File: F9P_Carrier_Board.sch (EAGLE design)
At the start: 82 parts, among them J4 U.FL, J5 QWIIC_RIGHT_ANGLE, J6 MICROMOD-2222-C, J8 JTAG, U1 U-BLOX_ZED-F9P, U5 AP7361C-33

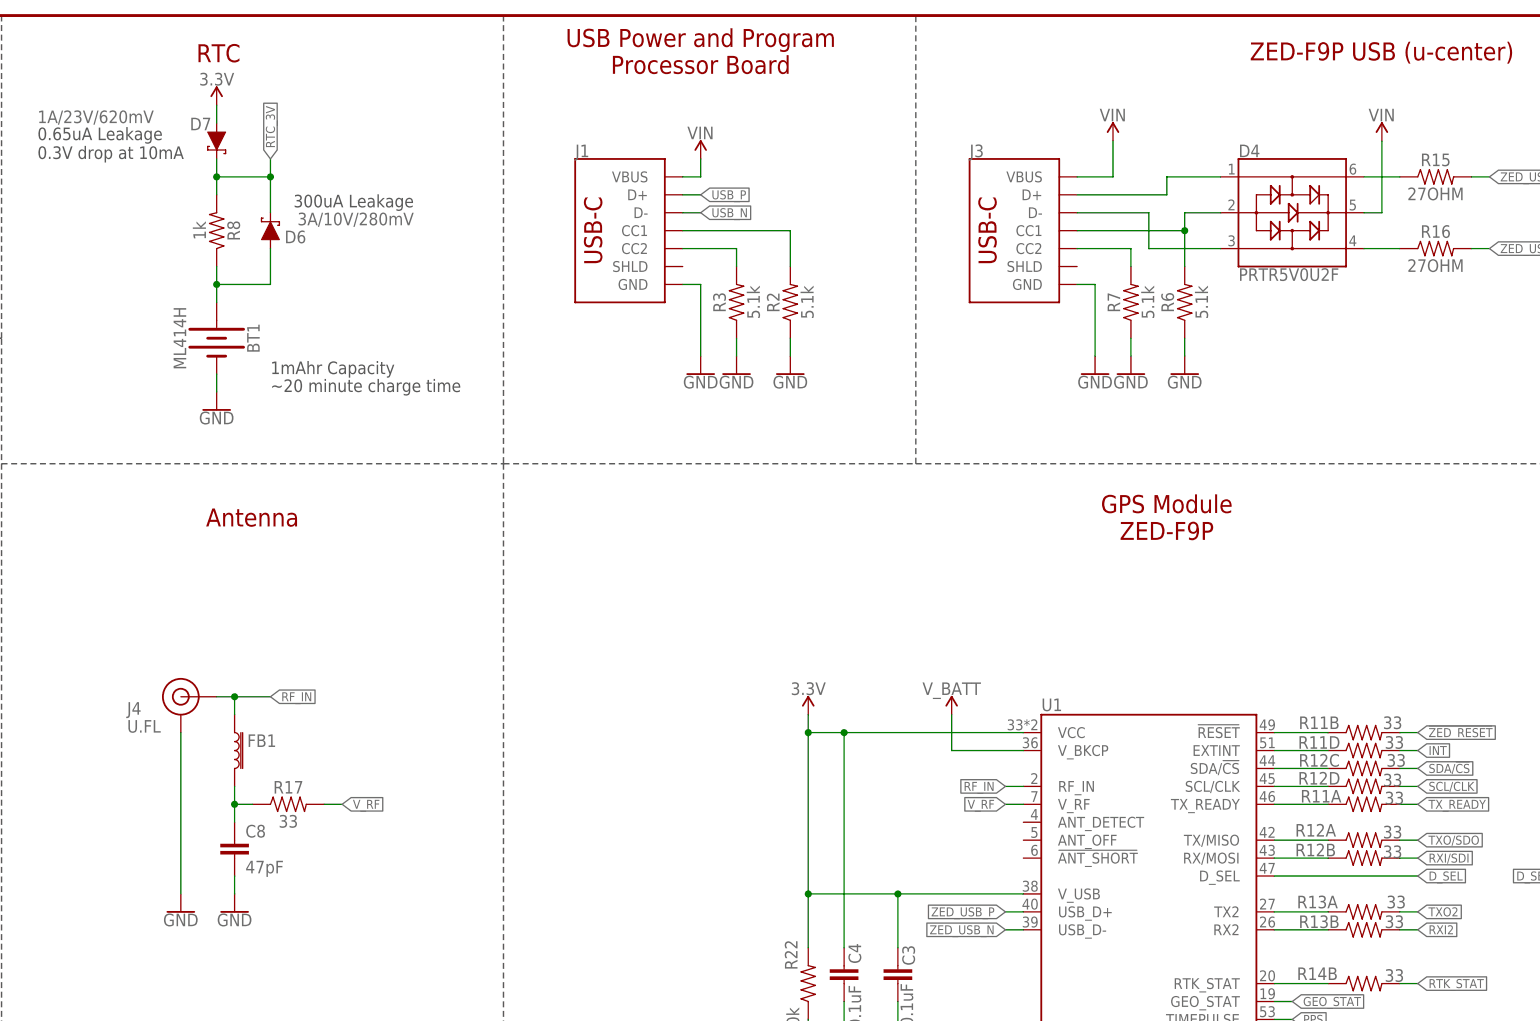
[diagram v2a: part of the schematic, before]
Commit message: Puts parts generally where they will be routed
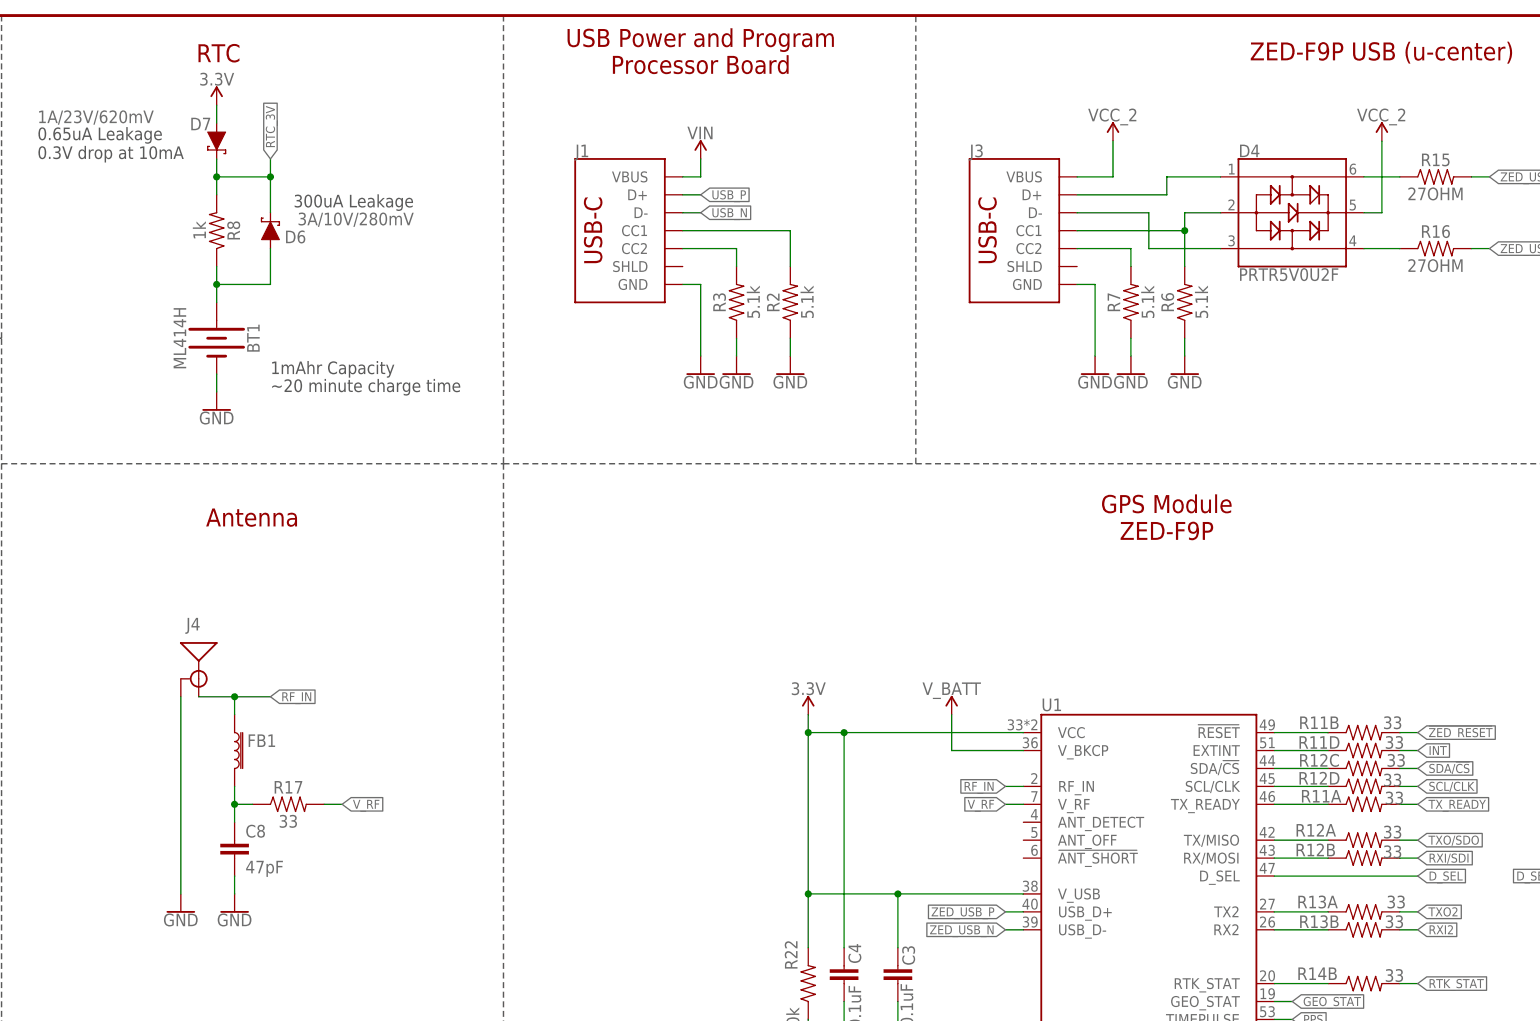
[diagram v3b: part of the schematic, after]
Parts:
- J4: device SparkFun-Connectors:U.FL2PIN -> SparkFun-RF:ANTENNA-GROUNDEDEDGE_SMA_SMD
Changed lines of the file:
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@@
 <part name="R14" library="SparkFun-Resistors" deviceset="33OHM_RA" device="-1206-1/16W-5%" value="33"/>
 <part name="SUPPLY2" library="SparkFun-PowerSymbols" deviceset="VIN" device=""/>
-<part name="SUPPLY3" library="SparkFun-PowerSymbols" deviceset="VIN" device=""/>
+<part name="SUPPLY3" library="SparkFun-PowerSymbols" deviceset="VCC_2" device=""/>
 <part name="R15" library="SparkFun-Resistors" deviceset="27OHM" device=""/>
 <part name="R16" library="SparkFun-Resistors" deviceset="27OHM" device=""/>
 <part name="D4" library="SparkFun-IC-Power" deviceset="PRTR5V0U2" device="F"/>
-<part name="SUPPLY5" library="SparkFun-PowerSymbols" deviceset="VIN" device=""/>
-<part name="J4" library="SparkFun-Connectors" deviceset="U.FL2PIN" device="" value="U.FL"/>
+<part name="SUPPLY5" library="SparkFun-PowerSymbols" deviceset="VCC_2" device=""/>
+<part name="J4" library="SparkFun-RF" deviceset="ANTENNA-GROUNDED" device="EDGE_SMA_SMD" value="U.FL"/>
 <part name="GND14" library="SparkFun-PowerSymbols" deviceset="GND" device=""/>
 <part name="GND17" library="SparkFun-PowerSymbols" deviceset="GND" device=""/>
@@
 <attribute name="VALUE" x="363.22" y="264.414" size="1.778" layer="96" align="bottom-center"/>
 </instance>
-<instance part="J4" gate="G$1" x="193.04" y="182.88" smashed="yes">
-<attribute name="NAME" x="185.42" y="180.34" size="1.778" layer="95"/>
-<attribute name="VALUE" x="185.42" y="177.8" size="1.778" layer="96"/>
+<instance part="J4" gate="G$1" x="195.58" y="185.42" smashed="yes" rot="MR0">
+<attribute name="NAME" x="195.834" y="192.278" size="1.778" layer="95" rot="MR0"/>
 </instance>
 <instance part="GND14" gate="1" x="193.04" y="152.4" smashed="yes">
@@
 <pinref part="J4" gate="G$1" pin="GND"/>
 <pinref part="GND14" gate="1" pin="GND"/>
-<wire x1="193.04" y1="177.8" x2="193.04" y2="154.94" width="0.1524" layer="91"/>
+<wire x1="193.04" y1="182.88" x2="193.04" y2="154.94" width="0.1524" layer="91"/>
 </segment>
 <segment>
@@
 <wire x1="320.04" y1="256.54" x2="325.12" y2="256.54" width="0.1524" layer="91"/>
 <wire x1="325.12" y1="256.54" x2="325.12" y2="261.62" width="0.1524" layer="91"/>
-<pinref part="SUPPLY3" gate="G$1" pin="VIN"/>
+<pinref part="SUPPLY3" gate="G$1" pin="VCC_2"/>
 </segment>
 <segment>
@@
 <wire x1="360.68" y1="251.46" x2="363.22" y2="251.46" width="0.1524" layer="91"/>
 <wire x1="363.22" y1="251.46" x2="363.22" y2="261.62" width="0.1524" layer="91"/>
-<pinref part="SUPPLY5" gate="G$1" pin="VIN"/>
+<pinref part="SUPPLY5" gate="G$1" pin="VCC_2"/>
 </segment>
 <segment>
@@
 <wire x1="200.66" y1="180.34" x2="200.66" y2="182.88" width="0.1524" layer="91"/>
 <pinref part="J4" gate="G$1" pin="SIGNAL"/>
-<wire x1="200.66" y1="182.88" x2="198.12" y2="182.88" width="0.1524" layer="91"/>
+<wire x1="200.66" y1="182.88" x2="195.58" y2="182.88" width="0.1524" layer="91"/>
 <junction x="200.66" y="182.88"/>
 <pinref part="FB1" gate="G$1" pin="1"/>

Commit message: Still situating the parts within the  board
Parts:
- removed J7: (no value), SparkFun-Connectors:CONN_08NO_SILK_DNP
- removed R14: 33, SparkFun-Resistors:33OHM_RA-1206-1/16W-5%
- J10: device SparkFun-Connectors:CONN_09NO_SILK -> SparkFun-Connectors:CONN_121X12_NO_SILK_KIT
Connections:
- removed net N$30: R14B.1, U1.RTK_STAT
- net 3.3V: now also J10.9, J9.3; no longer J10.8, J7.3
- net GND: now also J10.10; no longer J10.9, J7.1, J7.8
- net N$15: now also R11A.1, U1.EXTINT; no longer R11B.1, U1.!RESET!
- net N$16: now also R11B.1, U1.!SAFEBOOT!; no longer R11D.1, U1.EXTINT
- net N$19: now also R11C.1, U1.!RESET!; no longer R11A.1, U1.TX_READY
- net N$20: now also R11D.1, U1.TX_READY; no longer R11C.1, U1.!SAFEBOOT!
- net N$21: now also R12A.1, U1.SCL/CLK; no longer R12C.1, U1.SDA/!CS!
- net N$22: now also R12B.1, U1.SDA/!CS!; no longer R12D.1, U1.SCL/CLK
- net N$23: now also R12C.1, U1.RX/MOSI; no longer R12A.1, U1.TX/MISO
- net N$24: now also R12D.1, U1.TX/MISO; no longer R12B.1, U1.RX/MOSI
- net RTK_STAT: now also U1.RTK_STAT; no longer R14B.2
- net RXI/SDI: now also J10.11; no longer J7.5
- net SCL/CLK: now also J10.7; no longer J10.6, J7.7
- net SDA/!CS!: now also J10.8; no longer J10.7, J7.4
- net TXO/SDO: now also J10.12; no longer J7.6
- net VIN: now also J10.6; no longer J7.2
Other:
- moved on the sheet: R11A, R11B, R11C, R11D, R12A, R12B, R12C, R12D

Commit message: Moves parts to their final resting places (mostly)
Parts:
- C3, C4: device SparkFun-Capacitors:0.1UF-0402T-6.3V-10%-X7R -> SparkFun-Capacitors:0.1UF-0603-25V-5%
- C8: device SparkFun-Capacitors:47PF-0402-25V-5%-X7R -> SparkFun-Capacitors:47PF-0603-50V-5%
- R19, R20, R21: value 1KOHM-0402-1/16W-1% -> 1k; device SparkFun-Resistors:1KOHM-0402-1/16W-1% -> SparkFun-Resistors:1KOHM-0603-1/10W-1%
- R22: device SparkFun-Resistors:100KOHM-0402T-1/16W-1% -> SparkFun-Resistors:100KOHM-0603-1/10W-1%
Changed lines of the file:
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@@
 <part name="GND14" library="SparkFun-PowerSymbols" deviceset="GND" device=""/>
 <part name="GND17" library="SparkFun-PowerSymbols" deviceset="GND" device=""/>
-<part name="C8" library="SparkFun-Capacitors" deviceset="47PF" device="-0402-25V-5%-X7R" value="47pF"/>
+<part name="C8" library="SparkFun-Capacitors" deviceset="47PF" device="-0603-50V-5%" value="47pF"/>
 <part name="R17" library="SparkFun-Resistors" deviceset="33OHM" device="-0603-1/10W-1%" value="33"/>
 <part name="FB1" library="SparkFun-Coils" deviceset="FERRITE_BEAD-120_OHM" device="-0402T" value="FERRITE_BEAD-120_OHM-0402T"/>
-<part name="R19" library="SparkFun-Resistors" deviceset="1KOHM" device="-0402-1/16W-1%"/>
-<part name="R20" library="SparkFun-Resistors" deviceset="1KOHM" device="-0402-1/16W-1%"/>
+<part name="R19" library="SparkFun-Resistors" deviceset="1KOHM" device="-0603-1/10W-1%" value="1k"/>
+<part name="R20" library="SparkFun-Resistors" deviceset="1KOHM" device="-0603-1/10W-1%" value="1k"/>
 <part name="RTK" library="SparkFun-Jumpers" deviceset="JUMPER-SMT_2_NC_TRACE" device="_SILK" package3d_urn="urn:adsk.eagle:package:39281/1" value="JUMPER-SMT_2_NC_TRACE_SILK"/>
 <part name="PPS" library="SparkFun-Jumpers" deviceset="JUMPER-SMT_2_NC_TRACE" device="_SILK" package3d_urn="urn:adsk.eagle:package:39281/1" value="JUMPER-SMT_2_NC_TRACE_SILK"/>
@@
 <part name="D8" library="SparkFun-LED" deviceset="LED-BLUE" device="0603" value="BLUE"/>
 <part name="D9" library="SparkFun-LED" deviceset="LED-BLUE" device="0603" value="BLUE"/>
-<part name="R21" library="SparkFun-Resistors" deviceset="1KOHM" device="-0402-1/16W-1%"/>
+<part name="R21" library="SparkFun-Resistors" deviceset="1KOHM" device="-0603-1/10W-1%" value="1k"/>
 <part name="GEOF" library="SparkFun-Jumpers" deviceset="JUMPER-SMT_2_NC_TRACE" device="_SILK" package3d_urn="urn:adsk.eagle:package:39281/1" value="JUMPER-SMT_2_NC_TRACE_SILK"/>
 <part name="D10" library="SparkFun-LED" deviceset="LED-BLUE" device="0603" value="BLUE"/>
@@
 <part name="SUPPLY21" library="SparkFun-PowerSymbols" deviceset="3.3V" device=""/>
 <part name="BT2" library="SparkFun-Batteries" deviceset="ML414H_IV01E_BATTERY" device=""/>
-<part name="R22" library="SparkFun-Resistors" deviceset="100KOHM" device="-0402T-1/16W-1%" value="100k"/>
+<part name="R22" library="SparkFun-Resistors" deviceset="100KOHM" device="-0603-1/10W-1%" value="100k"/>
 <part name="GND29" library="SparkFun-PowerSymbols" deviceset="GND" device=""/>
 <part name="SUPPLY13" library="SparkFun-PowerSymbols" deviceset="3.3V" device=""/>
 <part name="SUPPLY22" library="SparkFun-PowerSymbols" deviceset="V_BATT" device=""/>
-<part name="C3" library="SparkFun-Capacitors" deviceset="0.1UF" device="-0402T-6.3V-10%-X7R" value="0.1uF"/>
-<part name="C4" library="SparkFun-Capacitors" deviceset="0.1UF" device="-0402T-6.3V-10%-X7R" value="0.1uF"/>
+<part name="C3" library="SparkFun-Capacitors" deviceset="0.1UF" device="-0603-25V-5%" value="0.1uF"/>
+<part name="C4" library="SparkFun-Capacitors" deviceset="0.1UF" device="-0603-25V-5%" value="0.1uF"/>
 <part name="LOGO1" library="SparkFun-Aesthetics" deviceset="SFE_LOGO_NAME" device=".1_INCH"/>
 <part name="FD2" library="SparkFun-Aesthetics" deviceset="FIDUCIAL" device="UFIDUCIAL"/>

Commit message: Routes more air wires - almost done
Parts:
- removed TP3: TEST-POINT3X5, SparkFun-Connectors:TEST-POINT3X5
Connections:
- removed net !SAFEBOOT: J10.3
- removed net GEOF_STAT: D10.A
- net !SAFEBOOT!: now also J10.3
- net GEO_STAT: now also D10.A
- net GND: now also D4.2
- net N$12: now also D4.3; no longer D4.1
- net N$13: now also D4.1; no longer D4.3
- net N$17: now also R15.1; no longer R16.1
- net N$6: no longer D4.2
- net N$9: now also R16.1; no longer R15.1
- net RXI2: no longer J6.TX2
- net SWDCK: no longer TP3.1
- net TXO2: no longer J6.RX2
- net VIN: no longer J1.VBUS, J3.VBUS
- net V_USB: now also J1.VBUS, J3.VBUS
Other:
- note added: "Board thickness: 1.6mm"
- note added: "Co-planar Calculation:"
- note added: "Copper Thickness (1oz): 1.4mil/0.035mm"
- note added: "Dielectric thickness: 1.46mm"
- note added: "Er: 4.58"
- note added: "No clean process"
- note added: "Polygon Isolation: .3mm"
- note added: "RF Trace Width: 1mm"
- moved on the sheet: C8, FB1, J4, R15, R16, R17

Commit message: Finishes initial routing
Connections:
- net INT: now also J6.G0/BUS0
- net RXI2: now also J6.RX2
- net TXO2: now also J6.TX2
- net TX_READY: now also J6.G1/BUS1
- net VIN: no longer D4.5, J10.6
- net V_USB: now also D4.5, J10.6
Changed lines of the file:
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@@
 <part name="SUPPLY8" library="SparkFun-PowerSymbols" deviceset="3.3V" device=""/>
 <part name="J8" library="SparkFun-Connectors" deviceset="CORTEX_JTAG_DEBUG_MINIMUM" device="_PTH" value="JTAG"/>
-<part name="SUPPLY5" library="SparkFun-PowerSymbols" deviceset="VIN" device=""/>
-<part name="SUPPLY12" library="SparkFun-PowerSymbols" deviceset="VIN" device=""/>
 <part name="SUPPLY9" library="SparkFun-PowerSymbols" deviceset="3.3V" device=""/>
 <part name="SUPPLY10" library="SparkFun-PowerSymbols" deviceset="V_USB" device=""/>
 <part name="SUPPLY2" library="SparkFun-PowerSymbols" deviceset="V_USB" device=""/>
+<part name="SUPPLY3" library="SparkFun-PowerSymbols" deviceset="V_USB" device=""/>
+<part name="SUPPLY5" library="SparkFun-PowerSymbols" deviceset="V_USB" device=""/>
 </parts>
 <sheets>
@@
 <attribute name="VALUE" x="129.54" y="48.514" size="1.778" layer="96" font="vector"/>
 </instance>
+<instance part="SUPPLY9" gate="G$1" x="307.34" y="66.04" smashed="yes">
+<attribute name="VALUE" x="307.34" y="68.834" size="1.778" layer="96" align="bottom-center"/>
+</instance>
+<instance part="SUPPLY10" gate="G$1" x="266.7" y="259.08" smashed="yes">
+<attribute name="VALUE" x="266.7" y="261.874" size="1.778" layer="96" align="bottom-center"/>
+</instance>
+<instance part="SUPPLY2" gate="G$1" x="325.12" y="259.08" smashed="yes">
+<attribute name="VALUE" x="325.12" y="261.874" size="1.778" layer="96" align="bottom-center"/>
+</instance>
+<instance part="SUPPLY3" gate="G$1" x="312.42" y="66.04" smashed="yes">
+<attribute name="VALUE" x="312.42" y="68.834" size="1.778" layer="96" align="bottom-center"/>
+</instance>
 <instance part="SUPPLY5" gate="G$1" x="363.22" y="261.62" smashed="yes">
 <attribute name="VALUE" x="363.22" y="264.414" size="1.778" layer="96" align="bottom-center"/>
-</instance>
-<instance part="SUPPLY12" gate="G$1" x="312.42" y="66.04" smashed="yes">
-<attribute name="VALUE" x="312.42" y="68.834" size="1.778" layer="96" align="bottom-center"/>
-</instance>
-<instance part="SUPPLY9" gate="G$1" x="307.34" y="66.04" smashed="yes">
-<attribute name="VALUE" x="307.34" y="68.834" size="1.778" layer="96" align="bottom-center"/>
-</instance>
-<instance part="SUPPLY10" gate="G$1" x="266.7" y="259.08" smashed="yes">
-<attribute name="VALUE" x="266.7" y="261.874" size="1.778" layer="96" align="bottom-center"/>
-</instance>
-<instance part="SUPPLY2" gate="G$1" x="325.12" y="259.08" smashed="yes">
-<attribute name="VALUE" x="325.12" y="261.874" size="1.778" layer="96" align="bottom-center"/>
 </instance>
 </instances>
@@
 <pinref part="SUPPLY2" gate="G$1" pin="V_USB"/>
 </segment>
+<segment>
+<wire x1="312.42" y1="48.26" x2="312.42" y2="66.04" width="0.1524" layer="91"/>
+<pinref part="J10" gate="G$1" pin="6"/>
+<wire x1="302.26" y1="48.26" x2="312.42" y2="48.26" width="0.1524" layer="91"/>
+<pinref part="SUPPLY3" gate="G$1" pin="V_USB"/>
+</segment>
+<segment>
+<pinref part="D4" gate="D1" pin="5"/>
+<wire x1="360.68" y1="251.46" x2="363.22" y2="251.46" width="0.1524" layer="91"/>
+<wire x1="363.22" y1="251.46" x2="363.22" y2="261.62" width="0.1524" layer="91"/>
+<pinref part="SUPPLY5" gate="G$1" pin="V_USB"/>
+</segment>
 </net>
 <net name="N$14" class="0">
@@
 <wire x1="38.1" y1="53.34" x2="35.56" y2="53.34" width="0.1524" layer="91"/>
 </segment>
-<segment>
-<pinref part="D4" gate="D1" pin="5"/>
-<wire x1="360.68" y1="251.46" x2="363.22" y2="251.46" width="0.1524" layer="91"/>
-<pinref part="SUPPLY5" gate="G$1" pin="VIN"/>
-<wire x1="363.22" y1="251.46" x2="363.22" y2="261.62" width="0.1524" layer="91"/>
-</segment>
-<segment>
-<pinref part="SUPPLY12" gate="G$1" pin="VIN"/>
-<wire x1="312.42" y1="48.26" x2="312.42" y2="66.04" width="0.1524" layer="91"/>
-<pinref part="J10" gate="G$1" pin="6"/>
-<wire x1="302.26" y1="48.26" x2="312.42" y2="48.26" width="0.1524" layer="91"/>
-</segment>
 </net>
 <net name="VIN/3" class="0">
@@
 <pinref part="J10" gate="G$1" pin="2"/>
 </segment>
+<segment>
+<pinref part="J6" gate="J1" pin="G0/BUS0"/>
+<wire x1="106.68" y1="144.78" x2="109.22" y2="144.78" width="0.1524" layer="91"/>
+<label x="109.22" y="144.78" size="1.27" layer="95" xref="yes"/>
+</segment>
 </net>
 <net name="SDA/!CS!" class="0">
@@
 <label x="312.42" y="45.72" size="1.27" layer="95" font="vector" rot="MR180" xref="yes"/>
 <pinref part="J10" gate="G$1" pin="5"/>
+</segment>
+<segment>
+<pinref part="J6" gate="J1" pin="G1/BUS1"/>
+<wire x1="106.68" y1="142.24" x2="109.22" y2="142.24" width="0.1524" layer="91"/>
+<label x="109.22" y="142.24" size="1.27" layer="95" xref="yes"/>
 </segment>
 </net>
@@
 <label x="368.3" y="152.4" size="1.27" layer="95" xref="yes"/>
 </segment>
+<segment>
+<pinref part="J6" gate="J1" pin="TX2"/>
+<wire x1="106.68" y1="152.4" x2="109.22" y2="152.4" width="0.1524" layer="91"/>
+<label x="109.22" y="152.4" size="1.27" layer="95" xref="yes"/>
+</segment>
 </net>
 <net name="RXI2" class="0">
@@
 <label x="368.3" y="149.86" size="1.27" layer="95" xref="yes"/>
 </segment>
-</net>
+<segment>
+<pinref part="J6" gate="J1" pin="RX2"/>
+<wire x1="106.68" y1="149.86" x2="109.22" y2="149.86" width="0.1524" layer="91"/>
+<label x="109.22" y="149.86" size="1.27" layer="95" xref="yes"/>
+</segment>
+</net>
